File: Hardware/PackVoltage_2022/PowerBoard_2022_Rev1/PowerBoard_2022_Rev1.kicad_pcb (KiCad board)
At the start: 2 copper layers, 330.2 x 177.8 mm, 361 parts, among them Q1 BUK7M8R5-40HX, Q10 BUK7M8R5-40HX, Q11 BUK7M8R5-40HX, Q12 BUK7M8R5-40HX, Q13 BUK7M8R5-40HX, Q14 BUK7M8R5-40HX, Q15 BUK7M8R5-40HX, Q16 BUK7M8R5-40HX, Q17 BUK7M8R5-40HX, Q18 BUK7M8R5-40HX, Q19 BUK7M8R5-40HX, Q2 BUK7M8R5-40HX, Q20 BUK7M8R5-40HX, Q21 BUK7M8R5-40HX, Q22 BUK7M8R5-40HX, Q3 BUK7M8R5-40HX, Q4 BUK7M8R5-40HX, Q5 BUK7M8R5-40HX, Q6 BUK7M8R5-40HX, Q7 BUK7M8R5-40HX, Q8 BUK7M8R5-40HX, Q9 BUK7M8R5-40HX, U1 LT1910, U10 OKI-78SR-12_1.0-W36-C, U11 OKI-78SR-12_1.0-W36-C, U12 OKI-78SR-12_1.0-W36-C, U13 OKI-78SR-12_1.0-W36-C, U14 OKI-78SR-12_1.0-W36-C, U15 OKI-78SR-12_1.0-W36-C, U16 OKI-78SR-12_1.0-W36-C, U17 OKI-78SR-12_1.0-W36-C, U18 OKI-78SR-12_1.0-W36-C, U19 OKI-78SR-12_1.0-W36-C, U2 INA281, U20 OKI-78SR-12_1.0-W36-C, U21 OKI-78SR-12_1.0-W36-C, U22 OKI-78SR-12_1.0-W36-C, U23 OKI-78SR-12_1.0-W36-C, U24 OKI-78SR-12_1.0-W36-C, U25 LT1910, U26 LT1910, U27 LT1910, U28 LT1910, U29 INA281, U3 LT1910, U30 INA281, U31 INA281, U32 INA281, U33 LT1910, U34 LT1910, U35 LT1910, U36 INA281, U37 INA281, U38 INA281, U39 TM4C129E_Launchpad, U4 INA281, U40 LT1910, U41 LT1910, U42 INA281, U43 INA281, U44 LT1910, U45 INA281, U46 LT1910, U47 INA281, U48 LT1910, U49 LT1910, U5 OKI-78SR-5_1.5-W36-C, U50 LT1910, U51 LT1910, U52 INA281, U53 INA281, U54 INA281, U55 INA281, U56 INA281, U57 LT1910, U58 INA281, U59 LT1910, U6 OKI-78SR-3.3_1.5-W36-C, U60 LT1910, U61 LT1910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

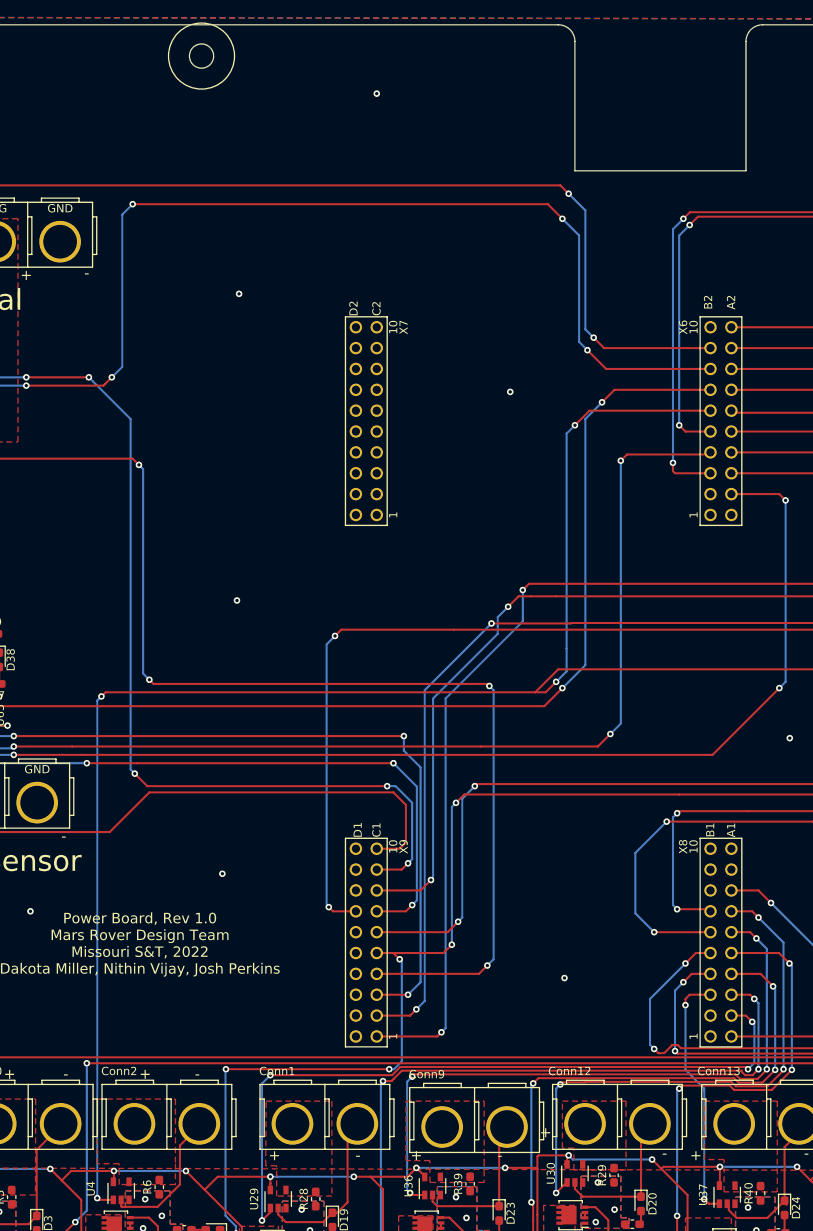
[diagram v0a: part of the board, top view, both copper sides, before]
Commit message: removed cutout for the tiva
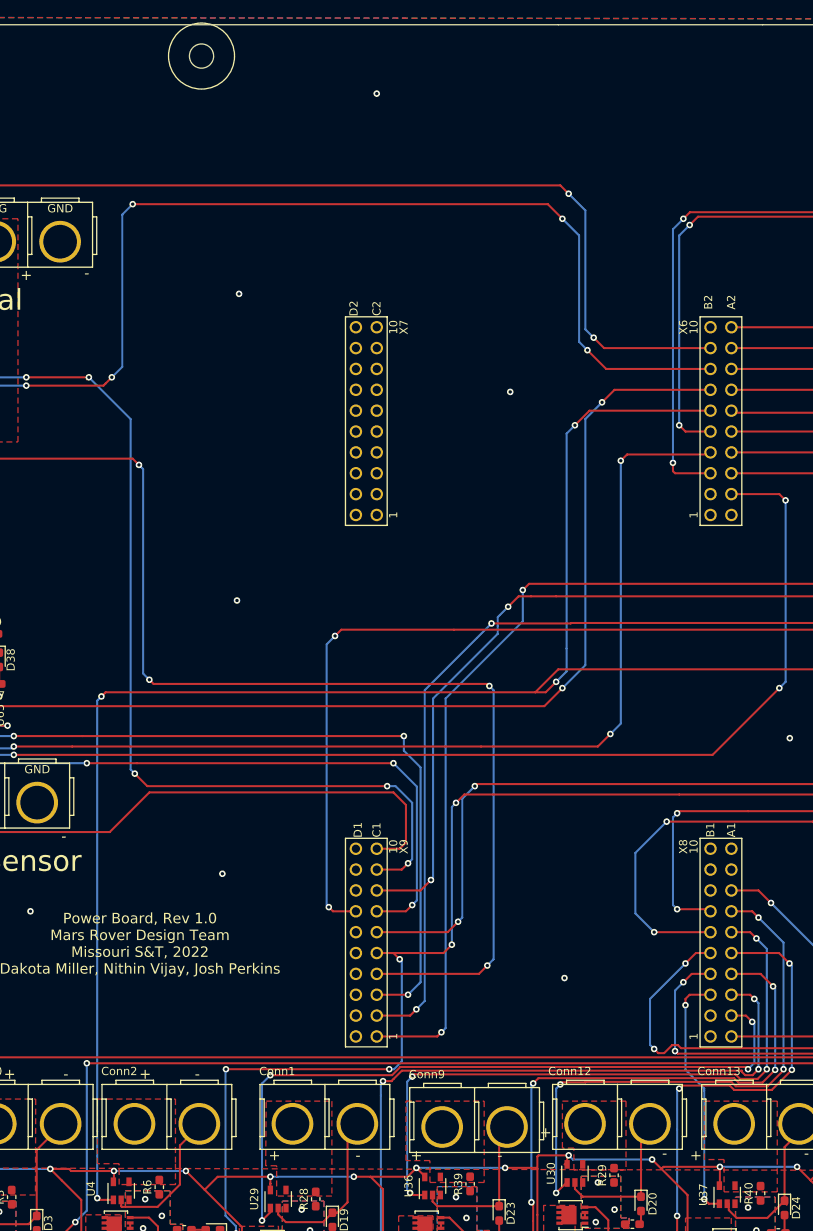
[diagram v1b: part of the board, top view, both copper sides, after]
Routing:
- net 5V: track 1036.4 -> 1037.4 mm
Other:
- outline, holes or cut-outs redrawn
- net class Default: trace_width 0.25 -> 0.254
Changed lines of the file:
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@@
-(kicad_pcb (version 20171130) (host pcbnew "(5.1.10)-1")
+(kicad_pcb (version 20171130) (host pcbnew "(5.1.4)-1")
   (general
     (thickness 1.6)
-    (drawings 98)
-    (tracks 1770)
+    (drawings 94)
+    (tracks 1771)
     (zones 0)
     (modules 361)
@@
   )
   (setup
-    (last_trace_width 0.25)
+    (last_trace_width 0.254)
     (trace_clearance 0.2)
     (zone_clearance 0.508)
@@
   (net_class Default "This is the default net class."
     (clearance 0.2)
-    (trace_width 0.25)
+    (trace_width 0.254)
     (via_dia 0.8)
     (via_drill 0.4)
@@
     )
   )
+  (gr_line (start 244.856 -190.5) (end 219.964 -190.5) (layer Edge.Cuts) (width 0.15))
   (gr_text "Power Board, Rev 1.0\nMars Rover Design Team\nMissouri S&T, 2022\nDakota Miller, Nithin Vijay, Josh Perkins" (at 169.037 -78.613) (layer F.SilkS)
     (effects (font (size 1.27 1.27) (thickness 0.3175)))
@@
   (gr_line (start 244.856 -190.5) (end 385.572 -190.5) (layer Edge.Cuts) (width 0.15))
   (gr_line (start 130.81 -190.5) (end 105.918 -190.5) (layer Edge.Cuts) (width 0.15))
-  (gr_line (start 221.996 -188.468) (end 221.996 -172.72) (layer Edge.Cuts) (width 0.15))
-  (gr_arc (start 219.964 -188.468) (end 221.996 -188.468) (angle -90) (layer Edge.Cuts) (width 0.15))
-  (gr_line (start 242.824 -172.72) (end 242.824 -188.468) (layer Edge.Cuts) (width 0.15))
-  (gr_line (start 221.996 -172.72) (end 242.824 -172.72) (layer Edge.Cuts) (width 0.15))
-  (gr_arc (start 244.856 -188.468) (end 244.856 -190.5) (angle -90) (layer Edge.Cuts) (width 0.15))
   (dimension 330.2 (width 0.15) (layer Dwgs.User)
     (gr_text "13.0000 in" (at 228.5815 -189.258764) (layer Dwgs.User)
@@
   (segment (start 253.1745 -47.3075) (end 250.698 -49.784) (width 0.25) (layer F.Cu) (net 8))
   (segment (start 165.862 -50.927) (end 160.655 -50.927) (width 0.25) (layer F.Cu) (net 8))
-  (segment (start 160.655 -50.927) (end 159.512 -49.784) (width 0.25) (layer F.Cu) (net 8))
   (segment (start 159.512 -49.784) (end 158.115 -51.181) (width 0.25) (layer F.Cu) (net 8))
   (segment (start 161.888001 -47.407999) (end 159.512 -49.784) (width 0.25) (layer F.Cu) (net 8))
@@
   (segment (start 217.424 -51.181) (end 217.424 -52.705) (width 0.25) (layer F.Cu) (net 8))
   (segment (start 217.424 -45.593) (end 217.424 -51.181) (width 0.25) (layer F.Cu) (net 8))
+  (segment (start 160.401 -51.181) (end 158.115 -51.181) (width 0.25) (layer F.Cu) (net 8))
+  (segment (start 160.655 -50.927) (end 160.401 -51.181) (width 0.25) (layer F.Cu) (net 8))
   (segment (start 299.212 -114.046) (end 298.958 -114.3) (width 0.25) (layer F.Cu) (net 9))
   (segment (start 304.038 -114.046) (end 299.212 -114.046) (width 0.25) (layer F.Cu) (net 9))

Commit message: Changed the footprint for the shunt resistors and loaded the netlist to the layout
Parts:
- removed C12, C22, C23, C24, C25, C35, C36, C37, C38, C47, C48, C49, C50, C59, C60, C61, C62: 22uF, Capacitor_THT:CP_Radial_D6.3mm_P2.50mm
- removed C15, C16, C26, C27, C28, C29, C39, C40, C41, C42, C51, C52, C53, C54, C63, C64, C65, C66: 10uF, Capacitor_SMD:C_0603_1608Metric_Pad1.05x0.95mm_HandSolder
- removed C19, C20, C30, C31, C32, C33, C43, C44, C45, C46, C55, C56, C57, C58, C67, C68, C69, C70: 47uF, Capacitor_THT:CP_Radial_D6.3mm_P2.50mm
- removed D10, D11, D12, D13, D14, D15, D16, D17, D18, D7, D8, D9: LED, LED_SMD:LED_0603_1608Metric_Pad1.05x0.95mm_HandSolder
- removed R10, R11, R12, R13, R14, R15, R16, R17, R18, R19, R20, R9: 1000, Resistor_SMD:R_0603_1608Metric_Pad1.05x0.95mm_HandSolder
- removed REF** (x2): 4_40_Hole, MRDT_Drill_Holes:4_40_Hole
- removed REF** (x4): 4_40_Hole, MRDT_Drill_Holes:4_40_Hole_Corner
- removed U10, U11, U12, U13, U14, U15, U16, U17, U18, U19, U20, U21, U22, U23, U24, U7, U8, U9: OKI-78SR-12_1.0-W36-C, MRDT_Devices:OKI_Horizontal
- C11: value 22uF -> 330uF; footprint Capacitor_THT:CP_Radial_D6.3mm_P2.50mm -> Capacitor_THT:CP_Radial_D12.5mm_P5.00mm
- F1, F10, F11, F12, F13, F14, F2, F8, F9: value 20A -> 20
- F4: value 3A -> 5A
- Q1, Q10, Q11, Q12, Q13, Q14, Q15, Q16, Q17, Q18, Q19, Q2, Q20, Q21, Q22, Q3, Q4, Q5, Q6, Q7, Q8, Q9: value BUK7M8R5-40HX -> BUK768R3-60E
- R28, R29, R3, R30, R32, R39, R40, R41, R46, R47, R50, R53, R6, R62, R63, R64, R65, R67, R70, R78, R79, R80: footprint Resistor_SMD:R_0603_1608Metric_Pad1.05x0.95mm_HandSolder -> Resistor_SMD:R_2512_6332Metric_Pad1.40x3.35mm_HandSolder
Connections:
- C100 pad 1: 12VCam1 -> PV1
- C101 pad 1: 12VDrive -> PV2
- C103 pad 1: 12VMultimedia -> PVMulti
- C108 pad 1: 12VNav -> PV1
- C109 pad 1: 12VNetSwitch -> PV2
- C11 pad 1: PV1 -> 12V
- C110 pad 1: 12VSciSensor -> PV2
- C34 pad 1: 12VA -> Net-(C34-Pad1)
- C87 pad 1: 12VSciAct -> PVAct
- C88 pad 1: 12VGimAct -> PVAct2
- C97 pad 1: 12VGimbal -> PV2
- C98 pad 1: 12VCam2 -> PV1
- C99 pad 1: 12VBBB -> PV1
- D5 pad 1: GND -> Net-(D5-Pad1)
- D6 pad 1: GND -> Net-(D6-Pad1)
- F3 pad 2: PV -> 12V
- F4 pad 1: PVMulti -> PV2
- F4 pad 2: PV -> 12V
- F5 pad 1: PV2 -> PVMulti
- F5 pad 2: PV -> 12V
- F6 pad 2: PV -> 12V
- F7 pad 2: PV -> 12V
- Q10 pad 5: 12VSciAct -> PVAct
- Q11 pad 5: 12VGimAct -> PVAct2
- Q14 pad 5: 12VGimbal -> PV2
- Q15 pad 5: 12VCam2 -> PV1
- Q16 pad 5: 12VBBB -> PV1
- Q17 pad 5: 12VCam1 -> PV1
- Q18 pad 5: 12VDrive -> PV2
- Q19 pad 5: 12VMultimedia -> PVMulti
- Q20 pad 5: 12VNav -> PV1
- Q21 pad 5: 12VNetSwitch -> PV2
- Q22 pad 5: 12VSciSensor -> PV2
- U40 pad 6: 12VSciAct -> PVAct
- U40 pad 8: 12VSciAct -> PVAct
- U41 pad 6: 12VGimAct -> PVAct2
- U41 pad 8: 12VGimAct -> PVAct2
- U48 pad 6: 12VGimbal -> PV2
- U48 pad 8: 12VGimbal -> PV2
- U49 pad 6: 12VCam2 -> PV1
- U49 pad 8: 12VCam2 -> PV1
- U50 pad 6: 12VBBB -> PV1
- U50 pad 8: 12VBBB -> PV1
- U51 pad 6: 12VCam1 -> PV1
- U51 pad 8: 12VCam1 -> PV1
- U57 pad 6: 12VDrive -> PV2
- U57 pad 8: 12VDrive -> PV2
- U59 pad 6: 12VMultimedia -> PVMulti
- U59 pad 8: 12VMultimedia -> PVMulti
- U60 pad 6: 12VNav -> PV1
- U60 pad 8: 12VNav -> PV1
- U61 pad 6: 12VNetSwitch -> PV2
- U61 pad 8: 12VNetSwitch -> PV2
- U62 pad 6: 12VSciSensor -> PV2
- U62 pad 8: 12VSciSensor -> PV2
- VR2 pad 7: 12VA -> Net-(C34-Pad1)
- VR2 pad 8: 12VA -> Net-(C34-Pad1)
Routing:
- removed copper zone on F.Cu, net 12VBBB
- removed copper zone on F.Cu, net 12VCam1
- removed copper zone on F.Cu, net 12VCam2
- removed copper zone on F.Cu, net 12VDrive
- removed copper zone on F.Cu, net 12VGimAct
- removed copper zone on F.Cu, net 12VGimbal
- removed copper zone on F.Cu, net 12VMultimedia
- removed copper zone on F.Cu, net 12VNav
- removed copper zone on F.Cu, net 12VNetSwitch
- removed copper zone on F.Cu, net 12VSciAct
- removed copper zone on F.Cu, net 12VSciSensor

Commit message: Loaded Netlist in layout and deleted all connections/wires
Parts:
- added VR3: Q36SR12020NRFA, MRDT_Devices:Q36SR12020NRFA, F.Cu at (118.6, -226.8)
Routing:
- net 5V: track 1037.4 -> 25.1 mm, vias 43 -> 2
- net GND: track 647.8 -> 41.3 mm, vias 40 -> 2
- net Current_Sensor_Aux: track 277.2 -> 0.00 mm, vias 6 -> 0
- net Driver_Spare: track 229.9 -> 0.00 mm, vias 8 -> 0
- net Current_Sensor_Nav: track 219.7 -> 0.00 mm, vias 6 -> 0
- net Current_Sensor_POE: track 215.8 -> 0.00 mm, vias 4 -> 0
- net Driver_Cam1: track 215.6 -> 0.00 mm, vias 4 -> 0
- net Driver_POE: track 214.8 -> 0.00 mm, vias 4 -> 0
- net Driver_Aux: track 197.0 -> 0.47 mm, vias 8 -> 0
- net Current_Sensor_BBB: track 195.9 -> 0.00 mm, vias 6 -> 0
- net Driver_Cam2: track 188.6 -> 0.00 mm, vias 6 -> 0
- net Driver_Gimbal: track 174.5 -> 0.00 mm, vias 6 -> 0
- net Current_Sensor_Drive: track 174.0 -> 0.00 mm, vias 8 -> 0
- net Driver_Drive: track 173.1 -> 0.00 mm, vias 8 -> 0
- net Driver_M7: track 172.5 -> 0.00 mm, vias 4 -> 0
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- removed copper zone on F.Cu, net PV

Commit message: Cleaned up board and set dimensions with new board size
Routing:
- removed copper zone on B.Cu, net GND
- removed copper zone on F.Cu, net GND
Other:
- board size 330.2 x 177.8 mm -> 279.4 x 152.4 mm

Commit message: Started organizing PV Circuits Layout
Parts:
- moved C6 375.2 mm to (519.4, -37.3), turned to 0 degrees
- moved U1 363.8 mm to (519.0, -43.6)
- moved F1 363.3 mm to (511.8, -23.8)
- moved R1 363.1 mm to (524.4, -45.1)
- moved C5 363.1 mm to (524.4, -40.8)
- moved Q1 362.2 mm to (510.8, -43.7), turned to 0 degrees
- moved Conn10 361.9 mm to (521.2, -64.7), turned to 270 degrees
- moved U2 360.7 mm to (509.8, -55.4), turned to 0 degrees
- moved R3 358.3 mm to (511.7, -50.2), turned to 0 degrees
- moved R2 350.3 mm to (505.7, -53.1), turned to 270 degrees
- moved D3 349.4 mm to (505.7, -56.9)
- moved C8 2.23 mm to (162.4, -34.5)
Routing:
- net Net-(Q1-Pad1): track 0.65 -> 4.25 mm, vias 3 -> 0
- net Net-(C5-Pad1): track 0.00 -> 3.25 mm
- net Net-(R1-Pad1): track 0.00 -> 2.70 mm
- net Net-(D3-Pad2): track 0.00 -> 2.07 mm
- removed copper zone on F.Cu, net Anderson_POE
- removed copper zone on B.Cu, net Net-(Q1-Pad1)

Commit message: Finished example for PV circuit and moved TIVA layout
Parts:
- moved U39 425.8 mm to (609.3, 149.9)
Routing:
- net Net-(Q1-Pad4): track 0.00 -> 12.2 mm, vias 0 -> 2
- net Anderson_POE: track 0.00 -> 3.20 mm
- added copper zone on F.Cu, net Anderson_POE
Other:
- rule trace_min: 0.2 -> 0.254
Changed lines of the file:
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@@
     (thickness 1.6)
     (drawings 75)
-    (tracks 106)
+    (tracks 120)
     (zones 0)
     (modules 261)
@@
     (zone_clearance 0.508)
     (zone_45_only no)
-    (trace_min 0.2)
+    (trace_min 0.254)
     (via_size 0.8)
     (via_drill 0.4)
@@
   )
   (module MRDT_Shields:TM4C129E_Launchpad_FULL_THT_TOP (layer F.Cu)
-    (at 242.316 -66.04 90)
+    (at 609.346 149.86 90)
     (fp_text reference U39 (at 122.174 -0.762 90) (layer F.SilkS) hide
       (effects (font (size 1 1) (thickness 0.15)))
@@
     (tags "capacitor handsolder")
     (attr smd)
-    (fp_text reference C6 (at 0 -1.43) (layer F.SilkS)
+    (fp_text reference C6 (at -0.127 1.905) (layer F.SilkS)
       (effects (font (size 1 1) (thickness 0.15)))
     )
@@
     (tags "LED handsolder")
     (attr smd)
-    (fp_text reference D3 (at 0 -1.43 270) (layer F.SilkS)
+    (fp_text reference D3 (at 0 -1.4605 270) (layer F.SilkS)
       (effects (font (size 1 1) (thickness 0.15)))
     )
@@
     (solder_mask_margin 0.05)
     (attr smd)
-    (fp_text reference Q1 (at 0 -2.55 180) (layer F.SilkS)
+    (fp_text reference Q1 (at -0.889 -2.667 180) (layer F.SilkS)
       (effects (font (size 1 1) (thickness 0.15)))
     )
@@
     (effects (font (size 1.27 1.27) (thickness 0.3175)))
   )
-  (gr_text - (at 525.8435 -86.106) (layer F.SilkS)
+  (gr_text - (at 525.018 -64.1985 90) (layer F.SilkS)
     (effects (font (size 1.27 1.27) (thickness 0.3175)))
   )
@@
     (effects (font (size 1.27 1.27) (thickness 0.3175)))
   )
-  (gr_text + (at 518.9855 -86.106) (layer F.SilkS)
+  (gr_text + (at 525.018 -57.3405 90) (layer F.SilkS)
     (effects (font (size 1.27 1.27) (thickness 0.3175)))
   )
@@
     (effects (font (size 2.54 2.54) (thickness 0.635)))
   )
-  (gr_text POE (at 521.7795 -30.560558 90) (layer F.SilkS)
+  (gr_text POE (at 508.635 -63.754) (layer F.SilkS)
     (effects (font (size 2.54 2.54) (thickness 0.635)))
   )
@@
   (segment (start 508.6965 -53.904) (end 508.6965 -50.2285) (width 0.254) (layer F.Cu) (net 80))
   (segment (start 508.6965 -54.483) (end 508.6965 -53.904) (width 0.254) (layer F.Cu) (net 80))
+  (via (at 509.397 -41.148) (size 0.8) (drill 0.4) (layers F.Cu B.Cu) (net 81))
+  (segment (start 509.259 -42.713) (end 509.259 -41.286) (width 0.254) (layer F.Cu) (net 81))
+  (segment (start 509.259 -41.286) (end 509.397 -41.148) (width 0.254) (layer F.Cu) (net 81))
+  (segment (start 509.397 -41.148) (end 512.826 -41.148) (width 0.254) (layer B.Cu) (net 81))
+  (segment (start 512.826 -41.148) (end 512.953 -41.148) (width 0.254) (layer B.Cu) (net 81))
+  (segment (start 512.953 -41.148) (end 513.588 -41.783) (width 0.254) (layer B.Cu) (net 81))
+  (segment (start 513.588 -41.783) (end 513.969 -42.164) (width 0.254) (layer B.Cu) (net 81))
+  (via (at 514.223 -45.593) (size 0.8) (drill 0.4) (layers F.Cu B.Cu) (net 81))
+  (segment (start 513.969 -42.164) (end 513.969 -45.339) (width 0.254) (layer B.Cu) (net 81))
+  (segment (start 513.969 -45.339) (end 514.223 -45.593) (width 0.254) (layer B.Cu) (net 81))
+  (segment (start 516.222 -45.593) (end 516.2855 -45.5295) (width 0.254) (layer F.Cu) (net 81))
+  (segment (start 514.223 -45.593) (end 516.222 -45.593) (width 0.254) (layer F.Cu) (net 81))
   (via (at 169.418 -43.942) (size 0.8) (drill 0.4) (layers F.Cu B.Cu) (net 83))
   (via (at 171.704 -45.466) (size 0.8) (drill 0.4) (layers F.Cu B.Cu) (net 83))
@@
   (segment (start 346.019 -157.318) (end 345.369 -157.318) (width 0.25) (layer F.Cu) (net 119))
   (segment (start 521.6855 -44.2595) (end 524.383 -44.2595) (width 0.254) (layer F.Cu) (net 124))
+  (segment (start 510.8965 -54.483) (end 511.6805 -54.483) (width 0.254) (layer F.Cu) (net 125))
+  (segment (start 511.6805 -54.483) (end 514.096 -54.483) (width 0.254) (layer F.Cu) (net 125))
   (segment (start 176.499252 -39.831557) (end 176.974252 -39.831557) (width 0.25) (layer F.Cu) (net 142))
   (segment (start 269.019 -39.37) (end 269.367 -39.37) (width 0.25) (layer F.Cu) (net 146))
@@
     (polygon
       (pts
-        (xy 510.0955 -35.4965) (xy 510.0955 -44.958) (xy 519.3665 -44.958) (xy 519.3665 -35.4965)
+        (xy 510.159 -35.52825) (xy 510.159 -44.98975) (xy 519.3665 -44.958) (xy 519.3665 -35.4965)
       )
     )
@@
     (polygon
       (pts
-        (xy 509.778 -43.053) (xy 509.778 -53.086) (xy 504.19 -53.086) (xy 504.19 -43.053)
+        (xy 509.651 -43.053) (xy 509.651 -53.086) (xy 504.19 -53.086) (xy 504.19 -43.053)
+      )
+    )
+  )
+  (zone (net 125) (net_name Anderson_POE) (layer F.Cu) (hatch edge 0.508)
+    (priority 2)
+    (connect_pads yes (clearance 0.508))
+    (min_thickness 0.254)
+    (fill yes (arc_segments 32) (thermal_gap 0.508) (thermal_bridge_width 0.508))
+    (polygon
+      (pts
+        (xy 513.08 -47.371) (xy 519.049 -47.371) (xy 519.049 -53.086) (xy 524.383 -53.086) (xy 524.383 -59.817)
+        (xy 513.08 -59.817)
       )
     )
